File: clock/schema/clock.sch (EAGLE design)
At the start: 13 parts, among them Q1 BC556

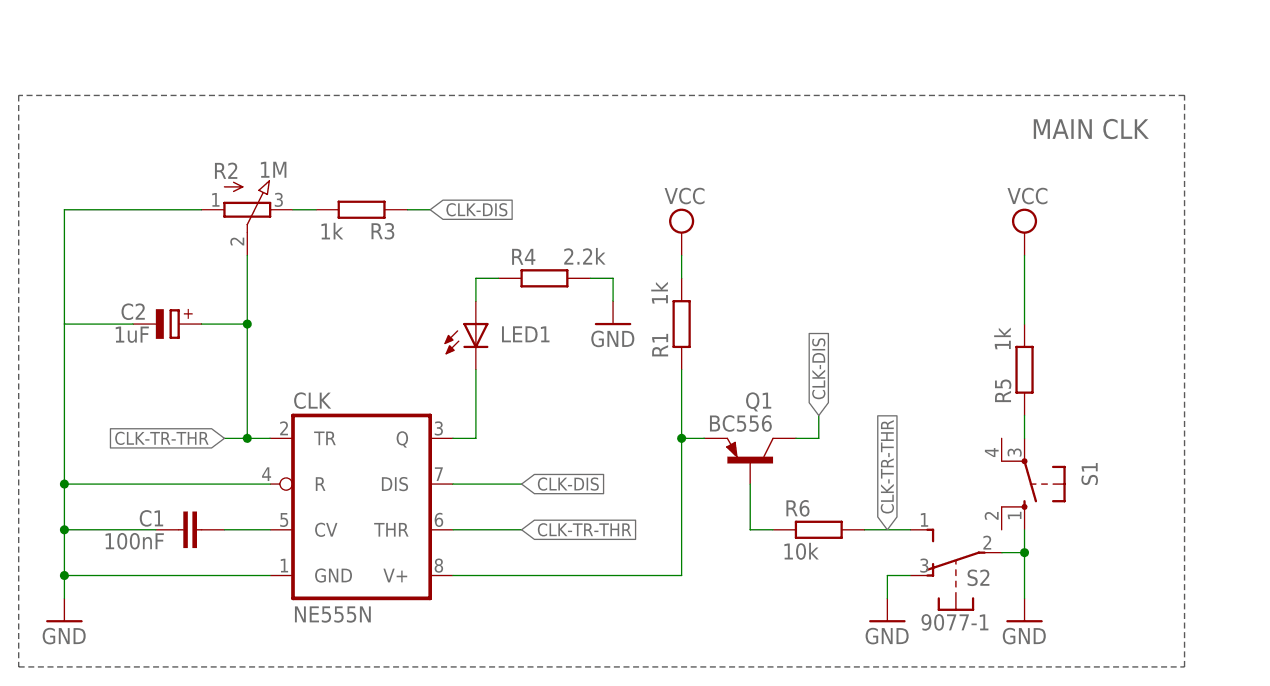
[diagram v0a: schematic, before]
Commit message: Added support for clock HALT signal
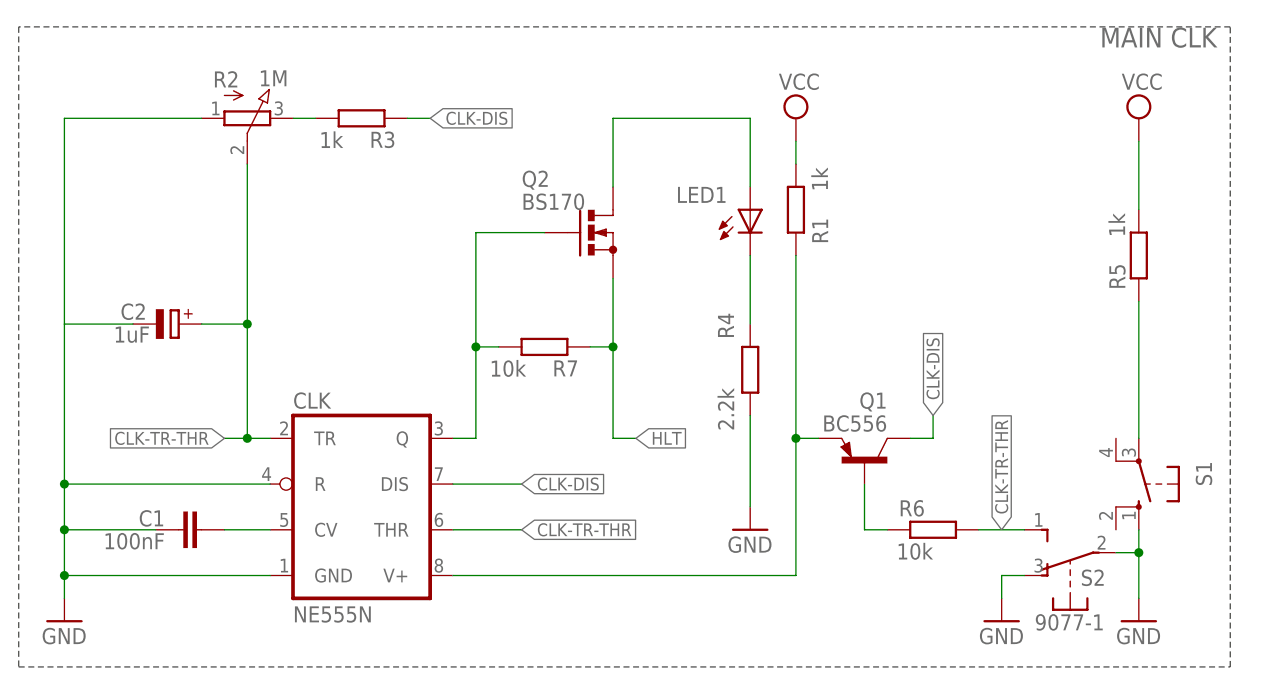
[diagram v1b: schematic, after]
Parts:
- added Q2: BS170, transistor-small-signal:BS170
- added R7: 10k, resistor:R-EU_0204/5
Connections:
- removed net CLK-Q: CLK.Q, LED1.C
- new net HLT: Q2.S, R7.1
- new net N$6: LED1.A, Q2.D
- new net Q: CLK.Q, Q2.G, R7.2
- net N$4: now also LED1.C; no longer LED1.A
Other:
- moved on the sheet: LED1, Q1, R1, R2, R3, R4, R5, R6, S1, S2
